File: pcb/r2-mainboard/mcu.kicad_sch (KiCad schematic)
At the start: 24 parts, among them J20 SWD+JTAG (DNP), SW20 SW, SW21 SW, SW22 SW, U20 STM32G0B1RCT6, Y20 32.768kHz

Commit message: R2: the six approved edits, and one of them was already done
Owner-approved 2026-08-19, KiCad closed for the pass.

1. R225 22k -> 20.5K/1%, LCSC C57105 (0402WGF2052TCE, UNI-ROYAL, the
   family the rest of the board already uses). Rendered and checked:
   R224 390k over R225 20.5k with R213 100k injecting VGH_DAC, so
   20.5||100 = 17.01k and VGH = 1.2 x (1 + 390/17.01) = 28.71 V at
   DAC = 0 -- exactly epd-port.md 10.3's target.
2. The five sense-divider caps that carried codes for the wrong
   capacitance -> C1523 (0402B102K500NT, 1 nF 50 V X7R, JLC Basic,
   5.3 M stock). One part covers both the 25 V and 50 V positions.
2b. R88/R224 -> C54920667 (HRC0402F3903DNTO, 390k 1%, 20 k stock).
   C25782 had 14 units against two per board. The owner found this one;
   both obvious alternatives were traps -- C23150 is 0603, and C44937
   is 3.9 ohm despite "390K" in its part number.
3. C147 set DNP rather than deleted. panel.md 7 had already ruled that
   J6.7/J6.44 stay; that covered the pins but not the capacitor on the
   dead net. DNP drops it from placement, keeps the topology of a frozen
   sheet untouched, and leaves the footprint if a future panel drives
   the rail. in_bom stays yes -- that is this board's convention for all
   13 DNP parts, so they show up flagged rather than vanishing.
4. Ten duplicate #PWR references renumbered to #PWR1112-1121 on the
   battery sheet, which was the colliding side in every case.
5. J3 was already deleted on 2026-08-15. No work needed.
6. Specter -> Reflow across 22 files: 14 sheets, 7 generators, the
   project file. .history/ deliberately untouched.

Verified as one change: netlist before and after has 518 nets with
identical pin membership, and epd_power and epd were rendered to PNG and
inspected.

Docs updated to match: epd-port.md 10 is applied rather than designed,
frontlight.md 1 loses the "9 in series is inferred" hedge (the vendor
listing confirms 2 x 9), and io-expansion.md 4's "only guess on this
sheet" is resolved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
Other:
- title: Glider-R2 / Specter mainboard -> Glider-R2 / Reflow mainboard
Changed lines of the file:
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@@
 	(paper "A3")
 	(title_block
-		(title "Glider-R2 / Specter mainboard")
+		(title "Glider-R2 / Reflow mainboard")
 		(date "2026-08-07")
 		(rev "A")

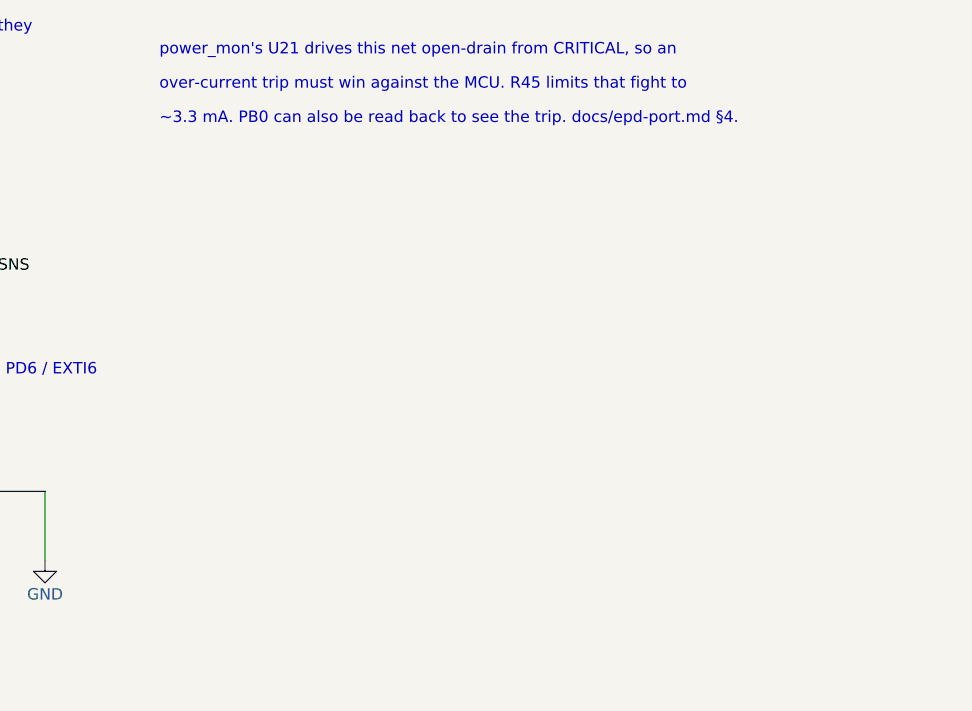
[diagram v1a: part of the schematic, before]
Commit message: R2: the SoM can now reset the MCU and force its bootloader (WP8 closed)
tools/patch_som_mcu_recovery.py applies mcu.md 5.8. On som, A59 and A60
lose their no-connects and gain SOM_MCU_NRST / SOM_MCU_BOOT0. On mcu,
three parts land on empty canvas at x>300:

  Q9    AO3400A  Transistor_FET:Q_NMOS_GSD, SOT-23, C347475
  R510  100k     gate pull-down
  R511  1k       series into PA14

NRST goes through the FET rather than straight to the pin, because the
MCU gates the SoM's own supply -- "SoM off, MCU alive" is the normal
standby state, and a direct tie would let an unpowered A59 clamp
MCU_NRST toward a dead VDDSHV_CANUART and hold the MCU in reset for
good. With Q9 the default is safe in every combination: gate low or SoM
unpowered leaves NRST to the STM32's internal pull-up.

BOOT0 needs no FET -- nothing on R2 drives PA14 high, so R40's pull-down
already defines the safe state, and R511 doubles as the contention limit
against an ST-LINK on the shared SWCLK pin.

Verified: 518 nets before and after; the only membership changes are
MCU_NRST += Q9.3, MCU_SWCLK += R511.2, GND += Q9.2/R510.2, plus the two
new nets and the two unconnected- entries that went away. Rendered to
PNG and inspected twice -- the first layout ran the MCU_NRST label
vertically into the BOOT0 row, so the drain now turns right first.

One trap recorded in mcu.md 5.8: set_sheet_pins re-lays every pin on a
root box, and the root's stubs and labels are positional, so adding two
pins silently rotated the membership of eighteen nets on the first run.
wire_root.py must be re-run after any sheet-pin change; the patch script
now does that itself and asserts on its exit code.

RM0444 (now in datasheets/) settles the factory question from source:
3.3.1 p.67, the EMPTY flag "allows easy programming of virgin devices by
the boot loader", so a blank board needs only an SD card. Riders: the
first flash needs a power cycle or OBL_LAUNCH to reload option bytes,
and the BOOT0 pin still earns its keep for recovery, w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
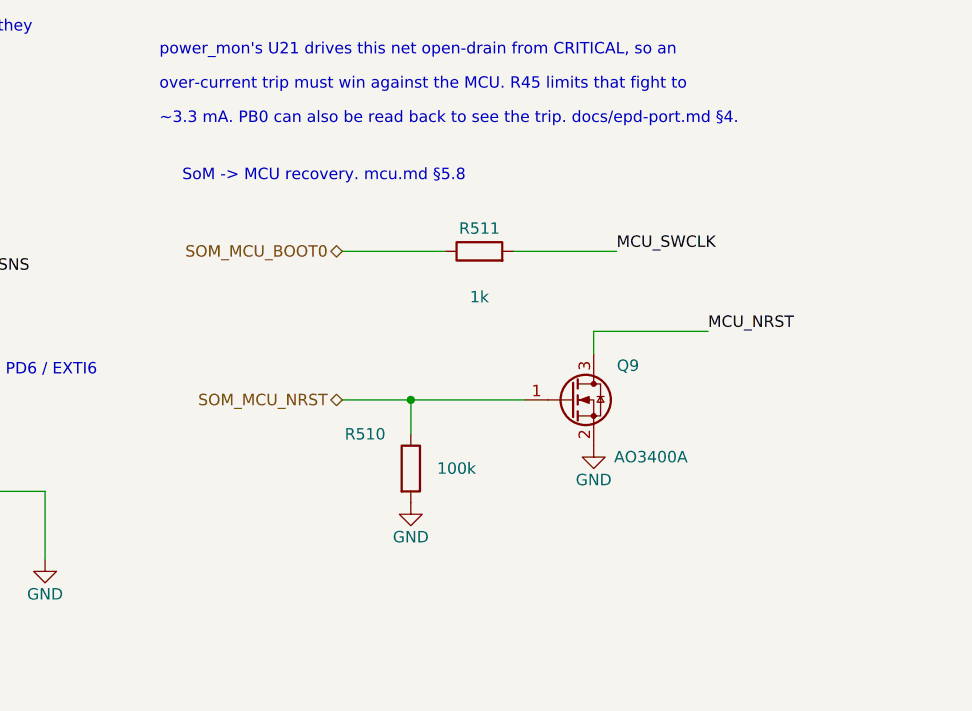
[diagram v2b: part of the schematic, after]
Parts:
- added Q9: AO3400A, Package_TO_SOT_SMD:SOT-23, symbol Transistor_FET:Q_NMOS_GSD
- added R510: 100k, Resistor_SMD:R_0402_1005Metric, symbol Device:R
- added R511: 1k, Resistor_SMD:R_0402_1005Metric, symbol Device:R
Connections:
- net GND: now also Q9.2 (S), R510.2
- net MCU_NRST: now also Q9.3 (D)
- net MCU_SWCLK: now also R511.2
- new net SOM_MCU_BOOT0: R511.1
- new net SOM_MCU_NRST: Q9.1 (G), R510.1
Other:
- note added: "SoM -> MCU recovery. mcu.md §5.8"

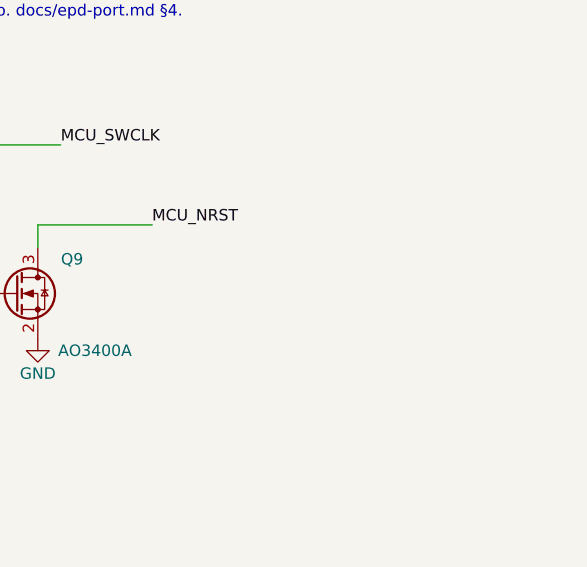
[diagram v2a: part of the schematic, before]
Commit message: R2: PG_SOM would have hung bring-up; plus the X1 refdes collision
From the review round of 2026-08-19. Verified each finding against the
datasheets and the schematic's own netlist before acting.

The one that matters -- PG_SOM. patch_mcu_pg_som.py told firmware to
enable PC8's internal pull-down so "no SoM" would read "not good".
X_PGOOD is open-drain with a 100k pull-up on the module (L-1038e.A5
Table 13, 5.4); the G0's internal pull-down is 25/40/55k (stm32g0b1.pdf
Table 55). Together: 3.3 x 40/140 = 0.94 V against V_IH 2.31 V, so PC8
reads low while the module asserts good, power.md 5.1 step 3 never
returns and MCU_EN_3V3 is never asserted. Not fixable in firmware -- the
pull-down strength is not configurable.

Leaving PC8 passive loses the case the pull-down was for: the PCM-071 is
a plug-in module and can be absent, not merely unpowered, and then
nothing biases the pin. R512 1M to GND covers all three cases; the good
case reads 3.00 V with 0.69 V of margin. Applied by
tools/patch_pg_som_pulldown.py -- 518 nets before and after, only
PG_SOM += R512.1 and GND += R512.2. Firmware requirement reverses: the
internal pull-down must now be DISABLED. mcu.md 5.9.

The review also missed one, and it is worse than the U40 nit: som.md,
power.md and mcu.md called the SoM connector X1, but X1 is a populated
part on this board -- the 33.33 MHz oscillator on fpga_config. "X1 C54"
parses as pin C54 of the oscillator. Renamed in som.md, layout.md and
system-overview.md, and the two "X1 C54" references fixed.

A blanket rename was wrong, though, and the first pass got it wrong:
all three X1 references in fpga.md really are the oscillator, including
"one more trace from X1", which is about USERCCLK replacing the internal
oscillator. fpga.md reverted. References inside PHYTEC quotations keep
X1, which is correct in PHYTEC's own namespace.

More pin-table drift than the review reported: pads 41, 43 and 49 are
wired to TOUCH_RST#, MCU_EN_TOUCH and MCU_EN_PEN but 3.1 still listed
all 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
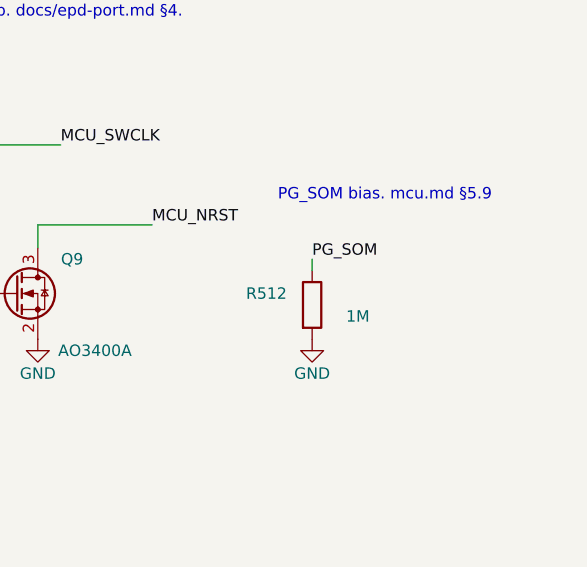
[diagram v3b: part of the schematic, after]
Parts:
- added R512: 1M, Resistor_SMD:R_0402_1005Metric, symbol Device:R
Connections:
- net GND: now also R512.2
- net PG_SOM: now also R512.1
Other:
- note added: "PG_SOM bias. mcu.md §5.9"
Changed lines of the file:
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@@
+		)
+	)
+	(text "PG_SOM bias. mcu.md §5.9"
+		(exclude_from_sim no)
+		(at 374.65 226.06 0)
+		(effects
+			(font
+				(size 1.27 1.27)
+			)
+			(justify left bottom)
+		)
+	)
+	(label "PG_SOM"
+		(at 378.46 232.41 0)
+		(effects
+			(font
+				(size 1.27 1.27)
+			)
+			(justify left bottom)
+		)
+	)
+	(wire
+		(pts
+			(xy 378.46 232.41) (xy 378.46 233.68)
+		)
+		(stroke
+			(width 0)
+			(type default)
+		)
+	)
+	(symbol
+		(lib_id "Device:R")
+		(at 378.46 237.49 0)
+		(unit 1)
+		(exclude_from_sim no)
+		(in_bom yes)
+		(on_board yes)
+		(dnp no)
+		(property "Reference" "R512"
+			(at 373.38 236.22 0)
+			(effects
+				(font
+					(size 1.27 1.27)
+				)
+			)
+		)
+		(property "Value" "1M"
+			(at 383.54 238.76 0)
+			(effects
+				(font
+					(size 1.27 1.27)
+				)
+			)
+		)
+		(property "Footprint" "Resistor_SMD:R_0402_1005Metric"
+			(at 378.46 237.49 0)
+			(hide yes)
+			(effects
+				(font
+					(size 1.27 1.27)
+				)
+			)
+		)
+		(property "Datasheet" ""
+			(at 378.46 237.49 0)
+			(hide yes)
+			(effects
+				(font
+					(size 1.27 1.27)
+				)
+			)
+		)
+		(property "Description" ""
+			(at 378.46 237.49 0)
+			(hide yes)
+			(effects
+				(font
+					(size 1.27 1.27)
+				)
+			)
+		)
+		(property "LCSC" "C26083"
+			(at 378.46 237.49 0)
+			(hide yes)
+			(effects
+				(font
+					(size 1.27 1.27)
+				)
+			)
+		)
+		(property "MPN" "0402WGF1004TCE"
+			(at 378.46 237.49 0)
+			(hide yes)
+			(effects
+				(font
+					(size 1.27 1.27)
+				)
+			)
+		)
+		(property "Manufacturer" "UNI-ROYAL"
+			(at 378.46 237.49 0)
+			(hide yes)
+			(effects
+				(font
+					(size 1.27 1.27)
+				)
+			)
+		)
+		(instances
+			(project "r2"
+				(path "/dee825bf-c2f1-415d-afdf-cf702072a6e8/a89f58f8-b115-4f71-9806-30f9bff6e587"
+					(reference "R512")
+					(unit 1)
+				)
+			)
+		)
+	)
+	(symbol
+		(lib_id "power:GND")
+		(at 378.46 241.3 0)
+		(unit 1)
+		(exclude_from_sim no)
+		(in_bom yes)
+		(on_board yes)
+		(dnp no)
+		(property "Reference" "#PWR1191"
+			(at 378.46 241.3 0)
+			(hide yes)
+			(effects
+				(font
+					(size 1.27 1.27)
+				)
+			)
+		)
+		(property "Value" "GND"
+			(at 378.46 245.11 0)
+			(effects
+				(font
+					(size 1.27 1.27)
+				)
+			)
+		)
+		(property "Footprint" ""
+			(at 378.46 241.3 0)
+			(hide yes)
+			(effects
+				(font
+					(size 1.27 1.27)
+				)
+			)
+		)
+		(property "Datasheet" ""
+			(at 378.46 241.3 0)
+			(hide yes)
+			(effects
+				(font
+					(size 1.27 1.27)
+				)
+			)
+		)
+		(property "Description" ""
+			(at 378.46 241.3 0)
+			(hide yes)
+			(effects
+				(font
+					(size 1.27 1.27)
+				)
+			)
+		)
+		(instances
+			(project "r2"
+				(path "/dee825bf-c2f1-415d-afdf-cf702072a6e8/a89f58f8-b115-4f71-9806-30f9bff6e587"
+					(reference "#PWR1191")
+					(unit 1)
+				)
+			)
 		)
 	)

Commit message: R2: two interrupts that could never fire, and the SoM footprint
The EXTI collisions mcu.md §3.4 found are applied. An EXTI line is picked
by the pin's *number*, so TOUCH_INT# on PC3 was fighting PD3 GAUGE_ALRT#
and PEN_INT# on PC6 was fighting PD6 QON_SNS -- as drawn neither touch nor
pen could raise an interrupt at all. Each swaps with an output, which needs
no line, so it costs nothing. FL_INT# gets PB12 at the same time, which was
frontlight.md §10.3's own first suggestion; §9's later push for PB7 was
wrong, because PC7 KEY_PREV# holds EXTI7.

518 -> 517 nets, the drop being the PB12 unconnected- pseudo-net, and
exactly five membership changes. Every hierarchical label in the project
now has a counterpart -- DANGLING_OK is empty and ERC excluding
footprint_link_issues is 32, down from 105.

The PCM-071 footprint is built rather than downloaded, because two drawings
have landed that over-determine it: Samtec's own vector land pattern (parsed
from the content stream, every measurement agreeing with a printed dimension
to under 1 um) and L-1038e.A5 Figure 7, which is a carrier-board drawing.
The trap it contains is that the alignment hole is NOT on the connector's
centreline -- it is 1.054 mm from one row and 5.118 from the other, and
Figure 7 dimensions the holes, so assuming a centred hole puts both
connectors 2.06 mm out. The check worth trusting is the one nothing forces:
the B and C rows land 0.982 and 0.998 mm inside the module's edges.

Also: U41's speed grade is settled -2 -- LCSC has no -3 in FTG256 at all,
and caster.xise's -3 is ISE's untouched default (valueState="default"), not
a choice anyone made. But -2's MCB is rated 667 Mb/s against the 666.67 this
design runs, so fpga.md §1.1 asks for one free ISE build before the order.

And a bring-up landmine: epd_pos_rails_good() accepts VGH <= 28.0 V while
R2's own R225 change puts it at 28.41 V nominal. A correctly built board
would fatal() at every EPD power-up. epd-port.md §10.5.

Co-Authored-By: Claude Op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
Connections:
- net MCU_EN_TOUCH: now also U20.38 (PC6); no longer U20.43 (PA9/PA11)
- net PEN_INT#: now also U20.43 (PA9/PA11); no longer U20.38 (PC6)
- net TOUCH_INT#: now also U20.41 (PD9); no longer U20.16 (PC3)
- net TOUCH_RST#: now also U20.16 (PC3); no longer U20.41 (PD9)
- net FL_INT#: now reaches U20.32 (PB12)
- no-connect marks 2 -> 1
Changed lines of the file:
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@@
 	)
 	(no_connect
-		(at 180.34 185.42)
-	)
-	(no_connect
 		(at 180.34 139.7)
 	)
@@
 	(hierarchical_label "MCU_EN_TOUCH"
 		(shape output)
-		(at 190.5 134.62 0)
+		(at 114.3 167.64 180)
 		(effects
 			(font
 				(size 1.27 1.27)
 			)
-			(justify left)
+			(justify right)
 		)
 	)
@@
 	(hierarchical_label "TOUCH_RST#"
 		(shape output)
-		(at 114.3 147.32 180)
+		(at 114.3 160.02 180)
 		(effects
 			(font
@@
 	(hierarchical_label "PEN_INT#"
 		(shape input)
-		(at 114.3 167.64 180)
+		(at 190.5 134.62 0)
 		(effects
 			(font
 				(size 1.27 1.27)
 			)
-			(justify right)
+			(justify left)
 		)
 	)
@@
 	(hierarchical_label "TOUCH_INT#"
 		(shape input)
-		(at 114.3 160.02 180)
+		(at 114.3 147.32 180)
 		(effects
 			(font
@@
 		)
 	)
+	(wire
+		(pts
+			(xy 180.34 185.42) (xy 190.5 185.42)
+		)
+		(stroke
+			(width 0)
+			(type default)
+		)
+	)
+	(hierarchical_label "FL_INT#"
+		(shape input)
+		(at 190.5 185.42 0)
+		(effects
+			(font
+				(size 1.27 1.27)
+			)
+			(justify left)
+		)
+	)
